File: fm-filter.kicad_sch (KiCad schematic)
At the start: 10 parts

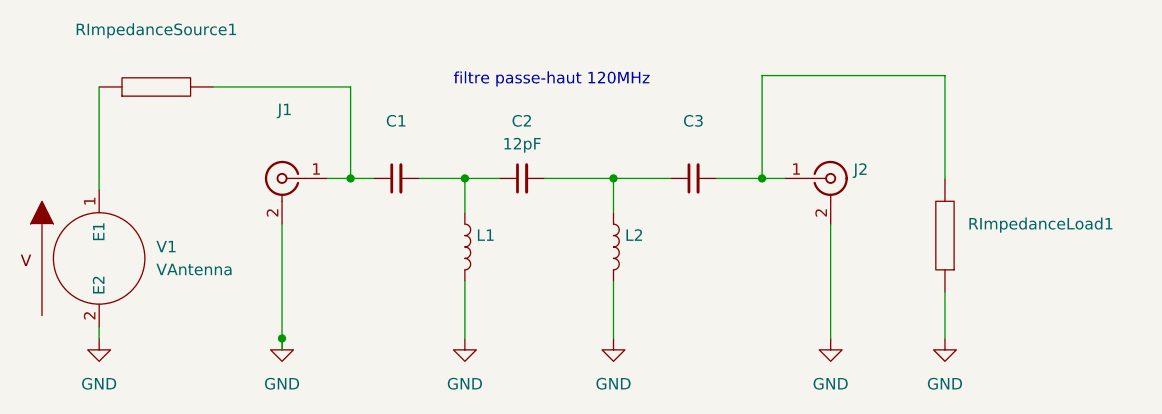
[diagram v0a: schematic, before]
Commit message: feat: separative wall
Migrate to KiCAD v7.
Update README.md with initial manual and online order tentative.
Move to a newer version with mounting holes and pin holes for the wall
support.
Test integration with aisler.net
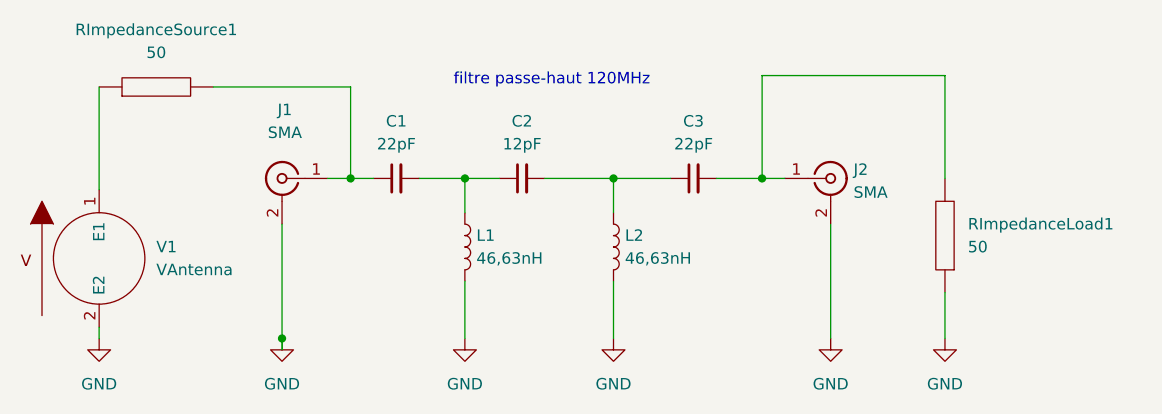
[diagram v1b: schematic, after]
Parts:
- C1, C3: value (none) -> 22pF; footprint (none) -> Capacitor_SMD:C_0805_2012Metric_Pad1.18x1.45mm_HandSolder; Spice_Model 22p -> (none); Spice_Netlist_Enabled Y -> (none); Spice_Primitive C -> (none)
- J1: value (none) -> SMA; footprint (none) -> Connector_Coaxial:SMA_Samtec_SMA-J-P-X-ST-EM1_EdgeMount; Spice_Netlist_Enabled N -> (none); Spice_Primitive X -> (none)
- J2: value (none) -> SMA; footprint (none) -> Connector_Coaxial:SMA_Samtec_SMA-J-P-X-ST-EM1_EdgeMount; Spice_Netlist_Enabled N -> (none)
- L1: value (none) -> 46,63nH; footprint (none) -> Inductor_THT:L_Axial_L9.5mm_D4.0mm_P12.70mm_Horizontal_Fastron_SMCC; Spice_Model 0.04836u -> (none); Spice_Netlist_Enabled Y -> (none); Spice_Primitive L -> (none)
- L2: value (none) -> 46,63nH; footprint (none) -> Inductor_THT:L_Axial_L9.5mm_D4.0mm_P12.70mm_Horizontal_Fastron_SMCC
- RImpedanceLoad1, RImpedanceSource1: value (none) -> 50
- V1: Spice_Model dc 0 ac 1 sin(0 1 100000000) -> (none); Spice_Netlist_Enabled Y -> (none); Spice_Primitive V -> (none)
